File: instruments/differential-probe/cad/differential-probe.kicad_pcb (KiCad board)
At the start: 4 copper layers, 150 x 70 mm, 111 parts, among them J3 BNC / PCB right-angle bulkhea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, Q1 MMBT3906,215, SW1 SPDT / ON-ON / gold / threaded, SW2 POWER / DPDT / ON-ON / thread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, SW3 RESET / NO, U1 OPA2810IDR, U12 OPA810IDR, U3 OPA2810IDR, U5 TLV1704AIPWR, U6 TLV1702AIDGKR, U7 CD4013BM96, U8 ADP7142AUJZ-R7, U9 ADP7182AUJZ-R7

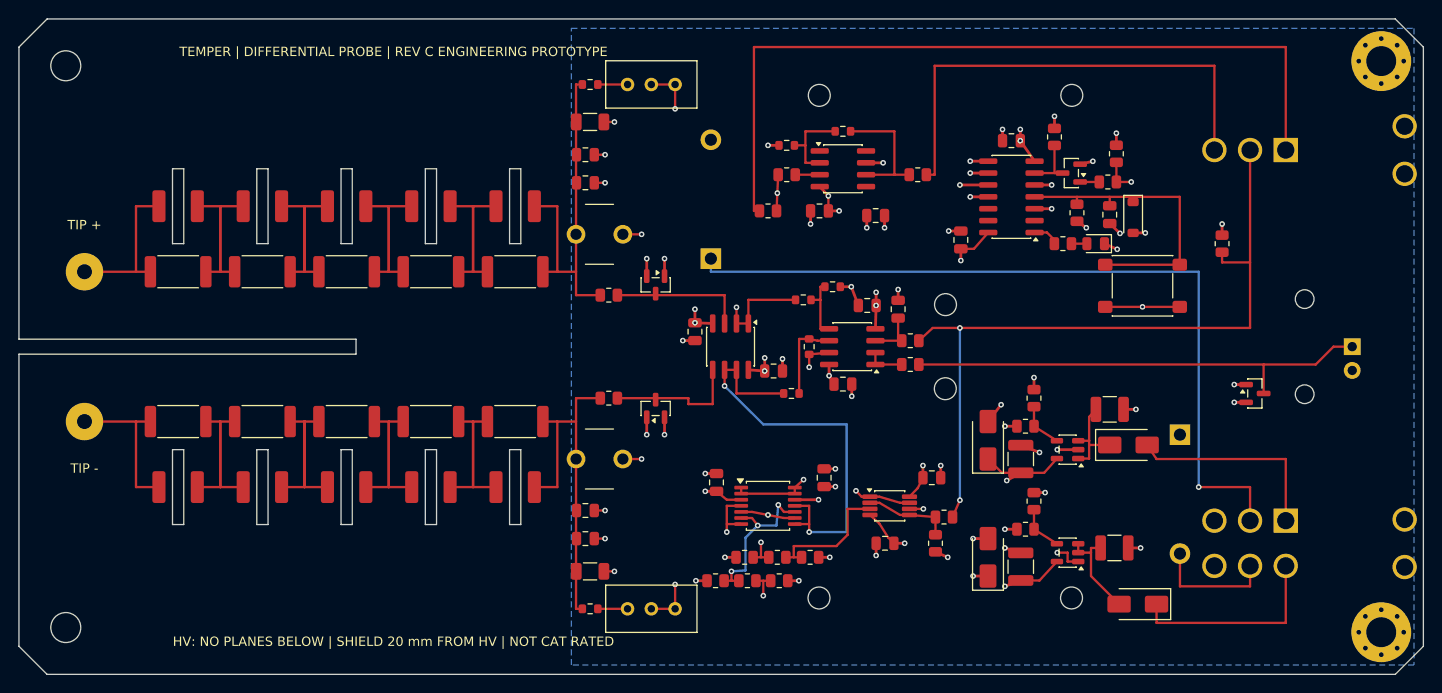
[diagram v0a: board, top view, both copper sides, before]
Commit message: feat(instruments): Rev C procurement export and board silk cleanup
Co-Authored-By: Claude Opus 5.5 <noreply@anthropic.com>
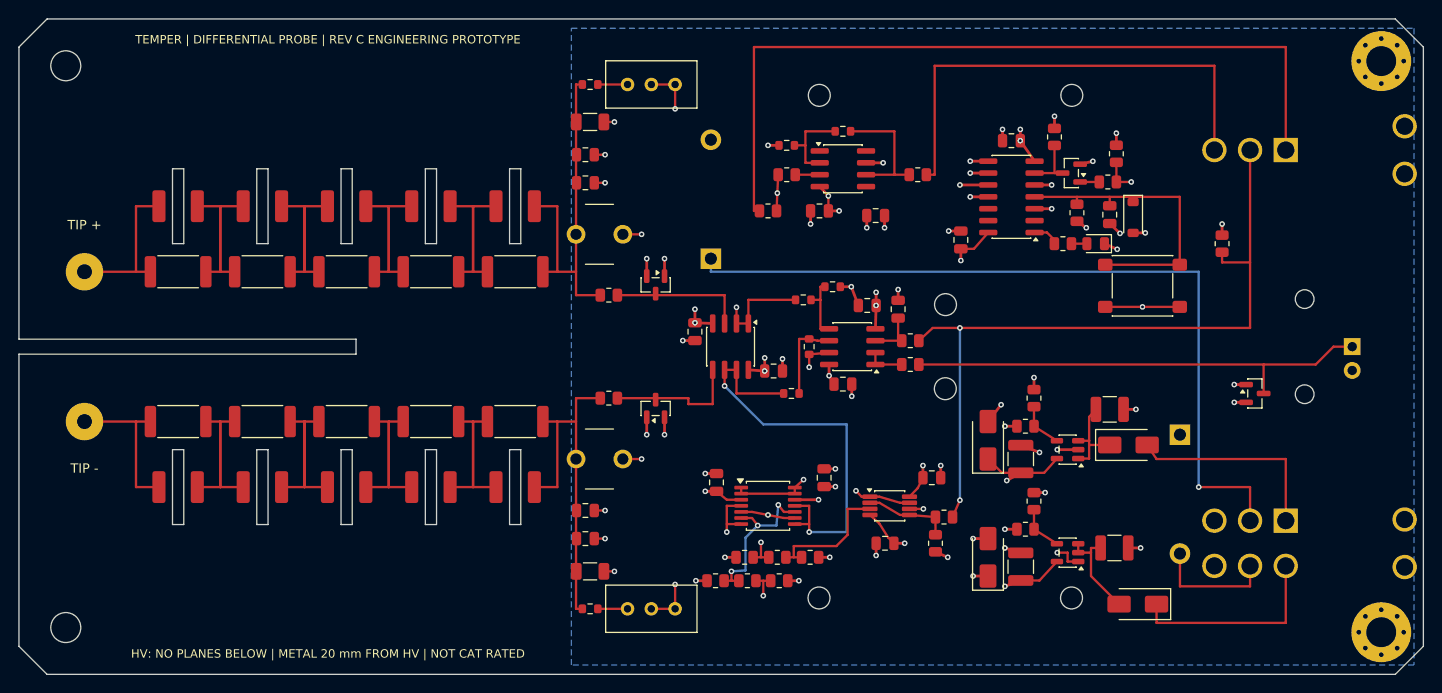
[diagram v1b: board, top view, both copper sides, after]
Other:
- board text added: "HV: NO PLANES BELOW | METAL 20 mm FROM HV | NOT CAT RATED"
- board text removed: "HV: NO PLANES BELOW | SHIELD 20 mm FROM HV | NOT CAT RATED"

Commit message: feat(probe): Rev C cost-down: HV12 divider, Yageo C0G, E-Switch toggles, Basic parts
Implements docs/cost-down.md with no layout change (pads, tracks and
courtyards identical to 5b9a9530b):

- HV divider: Uni-Royal HV121WF2004T4E (1 %, 1 W, 3 kV, JLC-stocked)
  replaces Stackpole HVCB2512BDE2M00; DC trim becomes 4.87 k 0.1 % +
  500 ohm (covers 1 % and 0.1 % strings, so HVCB stays a drop-in).
- Yageo CC1812JKNPOEBN330 (33 pF 3 kV NP0) and CC1206FKNPO9BN103
  (10 nF 1 % NP0) replace the KEMET parts.
- E-Switch 100SP1T1B5M7RE / 100DP1T1B1M7QEH replace the C&K toggles;
  footprints renamed ESwitch_100_M7_* from the E-Switch M7 drawing.
- Non-precision positions move to JLC Basic parts; C61 and the 10 uF
  move to stocked equivalents. Extended MPNs placed by JLC: 33 -> 24.
- check.rs: new MPN asserts, 1 %-string trim proof, divider TCR drift,
  1 W rating text with the 2+3 split fault case stated.

Two boards: components $535.81 -> $148.63 (ledger); with JLC fees,
PCB, ~$100 leads and enclosures $866.44 -> $448.20 (validation/cost.txt).

Co-Authored-By: Claude Opus 5.5 <noreply@anthropic.com>
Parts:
- D8: value 1N4148W-E3-18 -> 1N4148W
- Q1: value MMBT3906,215 -> MMBT5401
- R1, R2, R21, R22, R23, R24, R25, R3, R4, R5: value 2 MR / 0.1% -> 2 MR / 1% / 3 kV
- R11, R31: value 4.99 kR / 0.01% -> 4.87 kR / 0.1%
- RV1, RV2: value 50 R / set 12.50 R -> 500 R / set 132.5 R
- SW1: footprint Probe:CK_7101_AV2_SPDT -> Probe:ESwitch_100_M7_SPDT
- SW2: footprint Probe:CK_7201_AV2_DPDT -> Probe:ESwitch_100_M7_DPDT

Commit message: feat(probe): thru-hole PTS645 reset button, soldered by the owner
SW3 becomes the C&K PTS645SL43-2 LFS, the thru-hole twin of the SMT
PTS645SL43SMTR92 (same 6 x 6 mm body, 4.3 mm actuator, 130 gf; 50 mA /
12 V DC, 250 V AC dielectric, -40..85 C; no approval listed). JLC did not
stock the SMT part, so it was global-sourced: $20 commodity inspection plus
a $3.07 Extended feeder. Owner-soldered, both go. Strategy E: 24 -> 23
Extended, fees $104.17 -> $81.09, board total $271.34 -> $248.02.

- build.rs generates SW_Tactile_CK_PTS645_THT from the C&K "S STRAIGHT"
  drawing (4 x 1.0 mm holes on 6.5 x 4.5 mm, rows internally common) with a
  bottom courtyard over the tails.
- layout.rs moves SW3 to the panel strip (131.85, 46.25): over the old site
  its tails would hit BT1. SW_P drops to B.Cu under it; RESET arrives by an
  In2 hop; the +4V8 pins join the In2 pour. DRC 0/0, mirror and matched
  length checks unchanged.
- pcb-oracle gains a button-over-holder fixture: courtyard overlap fails.
- check_pcb.rs reports LV courtyard fill (top 32.8 %, was 32.9 %).
- cost.py routes the button to the owner; the baseline keeps it SMT.
  jlc_catalog.py --merge adds a part without re-dating the snapshot.

Function and reach unchanged: same nets, lid-hole access, new hole position.

Co-Authored-By: Claude Opus 5.5 <noreply@anthropic.com>
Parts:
- SW3: footprint Button_Switch_SMD:SW_SPST_PTS645Sx43SMTR92 -> Probe:SW_Tactile_CK_PTS645_THT
- moved SW3 21.3 mm to (131.8, 46.2)
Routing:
- net RESET: track 33.0 -> 52.4 mm, vias 0 -> 1
- net +4V8: track 54.5 -> 46.5 mm, vias 19 -> 18
- net SW_P: vias 0 -> 1

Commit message: feat(probe): Basic-part output filter, 220 R / 100 pF C0G
F3 of docs/fee-consolidation.md. R69 97.6 R RC0805FR becomes the
on-board Uni-Royal 0805W8F2200T5E and C61 180 pF CC0805JRNPO9BN181
becomes Samsung CL21C101JBANNNC (100 pF C0G 5 % 50 V, LCSC C1790,
Basic). Same 0805 footprints, no layout change. Pole 6.000 -> 5.900 MHz;
vendor model -3 dB 5.786 -> 5.628 MHz wide, 5.252 -> 5.131 MHz fine, no
peaking; 60 kHz phase -0.938 -> -0.953 deg wide. Strategy E: 23 -> 21
Extended, fees $81.09 -> $74.95, board total $248.02 -> $241.85.

Co-Authored-By: Claude Opus 5.5 <noreply@anthropic.com>
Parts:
- C61: value 180 pF -> 100 pF
- R69: value 97.6 R / 1% -> 220 R

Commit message: feat(probe): two-pole output filter with bandwidth jumper (C61 47 pF, C62 330 pF, JP1)
C61 drops to 47 pF C0G (CL21C470JBANNNC, Basic) and C62 330 pF C0G
(CL10C331JB8NNNC, Basic) shunts OUT at the BNC through the bridged
solder jumper JP1 (KiCad net-tie footprint, PCB copper, not in the BOM).
Cutting JP1 gives the ~11 MHz mode.

Vendor model (validation/spice/results.txt, interpolated): 5.768 MHz
wide / 5.273 MHz fine, no peaking, 60 kHz phase -1.000 / -1.241 deg;
JP1 cut 10.856 / 8.471 MHz. Full-band input-referred noise 172 / 116 mV
(was 373 / 141; tools/output_filter_study.py). The finding: U3A's
unfiltered tail dominated full-band noise (ideal U3A: 373 -> 157 mV).

ac.cir carries the JP1-cut case as a second run; candidates.cir keeps the
historical single-pole cases with JP=0. cost.py gains a feature layer
(FEATURE_SUBS/ADDS) and strategy H; +$0.20 two boards, no new Extended.
Gates: make check, pcb-check (DRC 0/0), pcb-oracle, simulate, export.sh.

Co-Authored-By: Claude Opus 5.5 <noreply@anthropic.com>
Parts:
- added C62: 330 pF, Capacitor_SMD:C_0603_1608Metric, F.Cu at (133.0, 41.2)
- added JP1: BW / bridged = 5.8 MHz, cut = 11 MHz, Jumper:SolderJumper-2_P1.3mm_Bridged_RoundedPad1.0x1.5mm, F.Cu at (133.0, 38.6)
- C61: value 100 pF -> 47 pF
- moved D3 3.20 mm to (128.8, 40.0)
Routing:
- net OUT_C: track 0.00 -> 2.62 mm
- net OUT: track 50.2 -> 51.9 mm
- net GND: track 64.2 -> 65.1 mm, vias 38 -> 39

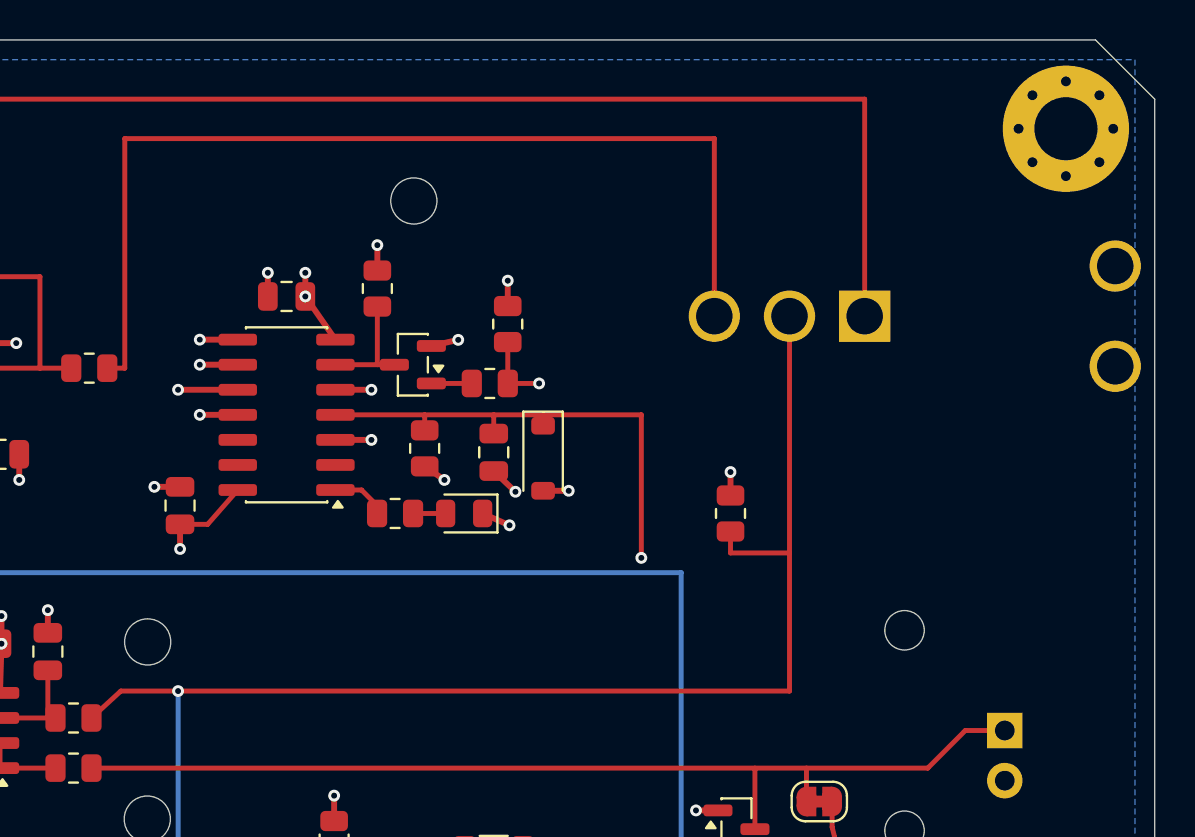
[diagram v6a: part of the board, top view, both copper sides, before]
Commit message: feat(probe): latched overvoltage trigger output on a second BNC (J4)
CD4013 flip-flop 2 (pins 8/10 on SET/RESET, /Q2 = TRIG_DRV) latches with
the warning LED and drives Q3 (MMBT5401) high-side through R110 22k
(0805W8F2202T5E, Basic); R112 470R (0805W8F4700T5E, Basic) feeds J4,
R111 10k holds 0 V idle, D10 BAV199 clamps TRIG_C. J4 cannot reach the
latch or comparators.

check.rs (worst-case rails/resistors): 4.445-4.920 V into 1 Mohm,
0.418-0.484 V into 50 ohm; Q3 forced beta <= 31 at the 11.1 mA short;
R112 <= 54 mW shorted; tolerated drive -7.5..+11.4 V. Latency estimate
1.64 us after OV_N (assumed Ceb 30 pF, 25 C maxima), plus TLV1704
460 ns typ: an estimate, not a bound, and not a peak-capture guarantee.

Panel order J4 7.72, SW1 21.36, J3 35.0, SW2 56.0; H1 moved to
(131.0, 31.2). LV top fill 33.0 -> 37.0 %. Cost +$7.42 two boards
(H - E now +$7.61), Extended 20 -> 20.
Gates: make check, pcb-check (DRC 0/0), pcb-oracle, simulate, export.sh.

Co-Authored-By: Claude Opus 5.5 <noreply@anthropic.com>
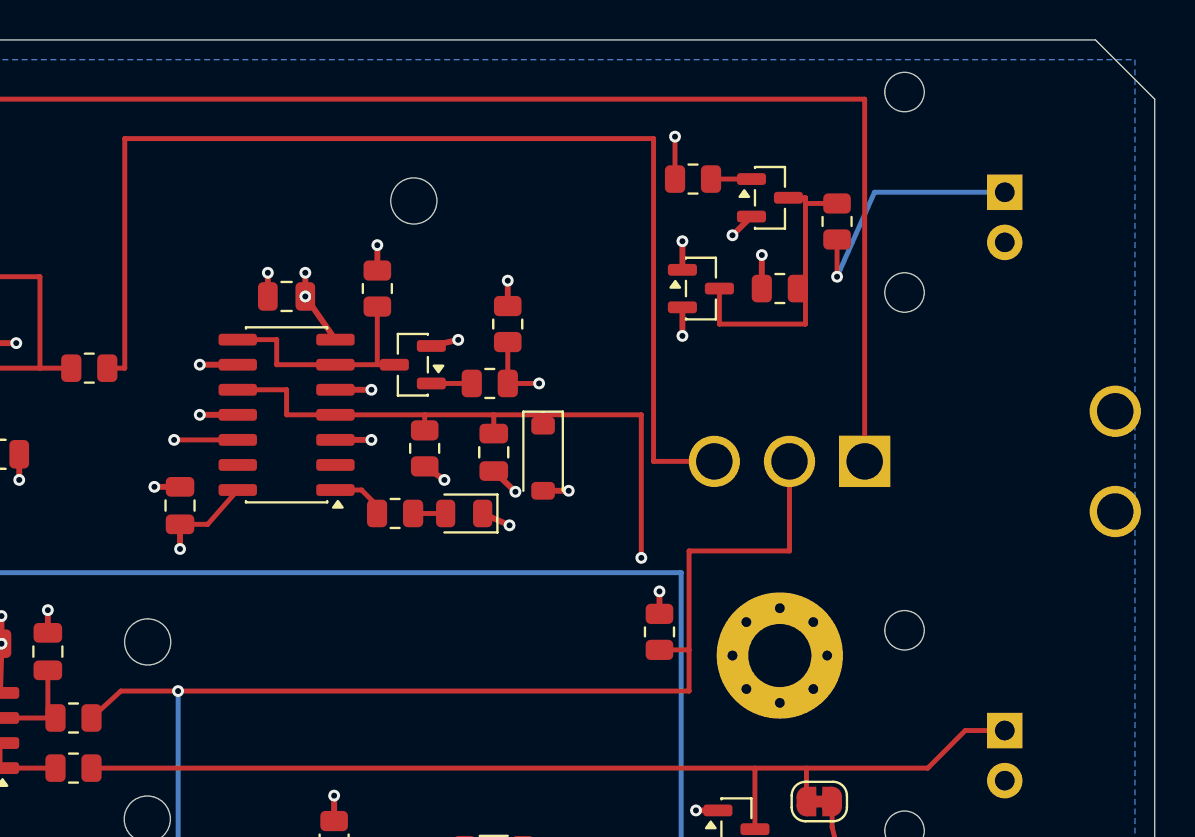
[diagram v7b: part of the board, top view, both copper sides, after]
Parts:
- added D10: BAV199,215, Package_TO_SOT_SMD:SOT-23, F.Cu at (127.0, 12.6)
- added J4: BNC / PCB right-angle bulkhead / 50 R, Probe:BNC_Amphenol_031-5431_Horizontal, F.Cu at (142.4, 7.72)
- added Q3: MMBT5401, Package_TO_SOT_SMD:SOT-23, F.Cu at (130.5, 8.00)
- added R110: 22 kR, Resistor_SMD:R_0805_2012Metric, F.Cu at (126.6, 7.05)
- added R111: 10 kR, Resistor_SMD:R_0805_2012Metric, F.Cu at (131.0, 12.6)
- added R112: 470 R, Resistor_SMD:R_0805_2012Metric, F.Cu at (133.9, 9.20)
- moved H1 30.4 mm to (131.0, 31.2)
- moved SW1 7.36 mm to (135.3, 21.4)
- moved R103 7.00 mm to (124.9, 30.0)
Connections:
- U7 pad 10: +4V8 -> RESET
- U7 pad 12: unconnected-(U7-/Q2-Pad12) -> TRIG_DRV
- U7 pad 8: -4V8 -> SET
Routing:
- net TRIG_DRV: track 0.00 -> 46.1 mm, vias 0 -> 2
- net TRIG_C: track 0.00 -> 15.4 mm
- net TRIG: track 0.00 -> 13.2 mm, vias 0 -> 1
- net SELECTED: track 79.4 -> 69.4 mm
- net WIDE_SEL: track 85.9 -> 93.2 mm
- net FINE_SEL: track 51.4 -> 58.8 mm
- net RESET: track 52.4 -> 58.7 mm
- net SET: track 5.94 -> 12.2 mm
- net GND: track 65.1 -> 68.2 mm, vias 39 -> 41
- net TRIG_B: track 0.00 -> 2.05 mm
- net -4V8: track 54.3 -> 52.4 mm, vias 27 -> 26
- net +4V8: track 46.3 -> 46.1 mm, vias 18 -> 19

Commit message: feat(probe): per-range analog zero trims (RV3 wide, RV4 fine)
Two 20 k Bourns 3296W-1-203LF pots across the rails (owner-soldered THT,
C34845): RV3 injects into WIDE_SEL through R113 10 k against R101's
49.9 R; RV4 into U12's inverting node through R114 66.5 k. Both act
after the subtraction, so CMRR is untouched; clockwise raises the output.

check.rs: reach +/-22.6 / +/-139.3 mV at the BNC vs worst untrimmed
19.2 / 92.7 mV; trimmed selected-path zero <= 9.58 / 44.39 mV over
-25..85 C (OPA2810 13 uV/C, OPA810 10 uV/C, full rail spread, 1 % pot
ratio shift + CRV). budget.rs gains warning_with(); acceptance tightens
to +/-10 / +/-45 mV, late trip 1341.8 -> 1326.5 V wide, 289.79 ->
272.45 V fine. Cost of the loading: wide gain -0.33 % (mid-travel),
fine +0.56 %; wide calibrated-gain acceptance 98.81 -> 98.82 %.
SPICE (R113/R114 loads in probe_lv.inc): 5.769 / 5.267 MHz, no peaking.

Placement x 65.9..71.3 beside the tap cells (tails clear of the holders);
wipers run on In2 under In1 GND. LV top fill 37.0 -> 38.9 %.
Cost +$3.54 two boards, Extended 20 -> 20.
Gates: make check, pcb-check (DRC 0/0), pcb-oracle, simulate, export.sh.

Co-Authored-By: Claude Opus 5.5 <noreply@anthropic.com>
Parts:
- added R113: 10 kR, Resistor_SMD:R_0805_2012Metric, F.Cu at (76.4, 19.5)
- added R114: 66.5 kR, Resistor_SMD:R_0805_2012Metric, F.Cu at (82.0, 10.5)
- added RV3: 20 kR zero trim, Potentiometer_THT:Potentiometer_Bourns_3296W_Vertical, F.Cu at (68.6, 57.6)
- added RV4: 20 kR zero trim, Potentiometer_THT:Potentiometer_Bourns_3296W_Vertical, F.Cu at (68.6, 12.4)
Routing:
- net TRIM_W: track 0.00 -> 39.2 mm, vias 0 -> 1
- net TRIM_F: track 0.00 -> 15.6 mm, vias 0 -> 1
- net GAIN5_FB: track 9.24 -> 11.8 mm
- net WIDE_SEL: track 93.2 -> 94.4 mm
